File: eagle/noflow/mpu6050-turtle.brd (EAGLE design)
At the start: 52.4 x 77.6 mm, 21 parts

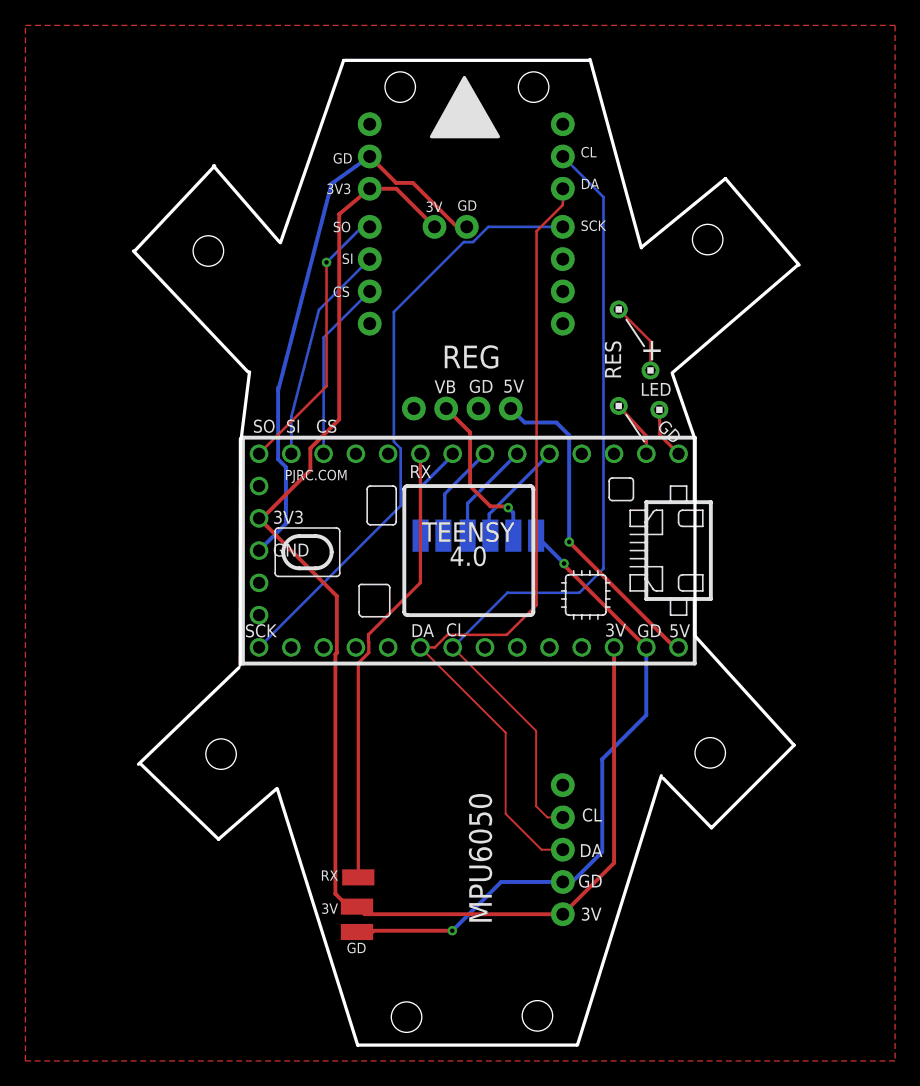
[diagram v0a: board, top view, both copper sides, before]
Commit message: Added no-flow board
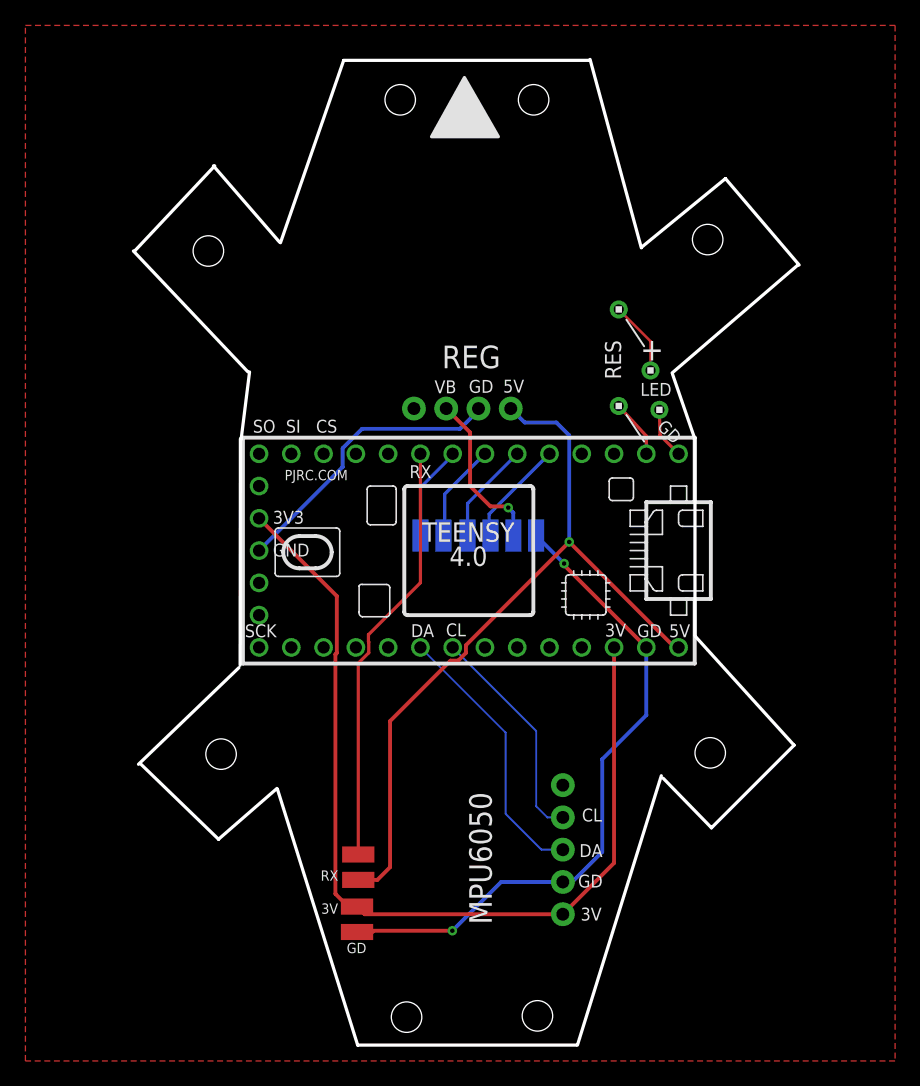
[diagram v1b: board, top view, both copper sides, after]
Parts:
- removed PMW1, PMW2: (no value), SparkFun-Connectors:1X04_NO_SILK
- removed PMW3: (no value), SparkFun-Connectors:1X02_NO_SILK
- removed VL1, VL2: (no value), SparkFun-Connectors:1X03_NO_SILK
- added 3V1: (no value), wirepad:SMD1,27-2,54
- moved RX 1.80 mm to (26.0, 16.0)
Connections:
- net 3V3: no longer PMW3.1, VL2.1
- net 5V: now also 3V1.1
- net CS: no longer PMW2.3
- net GND: no longer PMW3.2, VL2.2
- net MISO: no longer PMW2.1
- net MOSI: no longer PMW2.2
- net SCK: no longer PMW1.1
- net SCL: no longer VL1.2
- net SDA: no longer VL1.1
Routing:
- net SCL: track 65.9 -> 17.7 mm
- net SCK: track 47.6 -> 0.29 mm
- net SDA: track 65.7 -> 21.5 mm
- net 3V3: track 110.0 -> 74.1 mm
- net 5V: track 25.8 -> 60.0 mm
- net MISO: track 21.8 -> 0.00 mm, vias 1 -> 0
- net GND: track 97.5 -> 75.9 mm
- net MOSI: track 17.3 -> 0.00 mm
- net CS: track 14.3 -> 0.00 mm
- net RX: track 35.4 -> 33.6 mm
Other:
- board text removed: "PMW3901"
- board text removed: "VL53LL1"

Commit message: modified:   eagle/noflow/mpu6050-turtle.brd
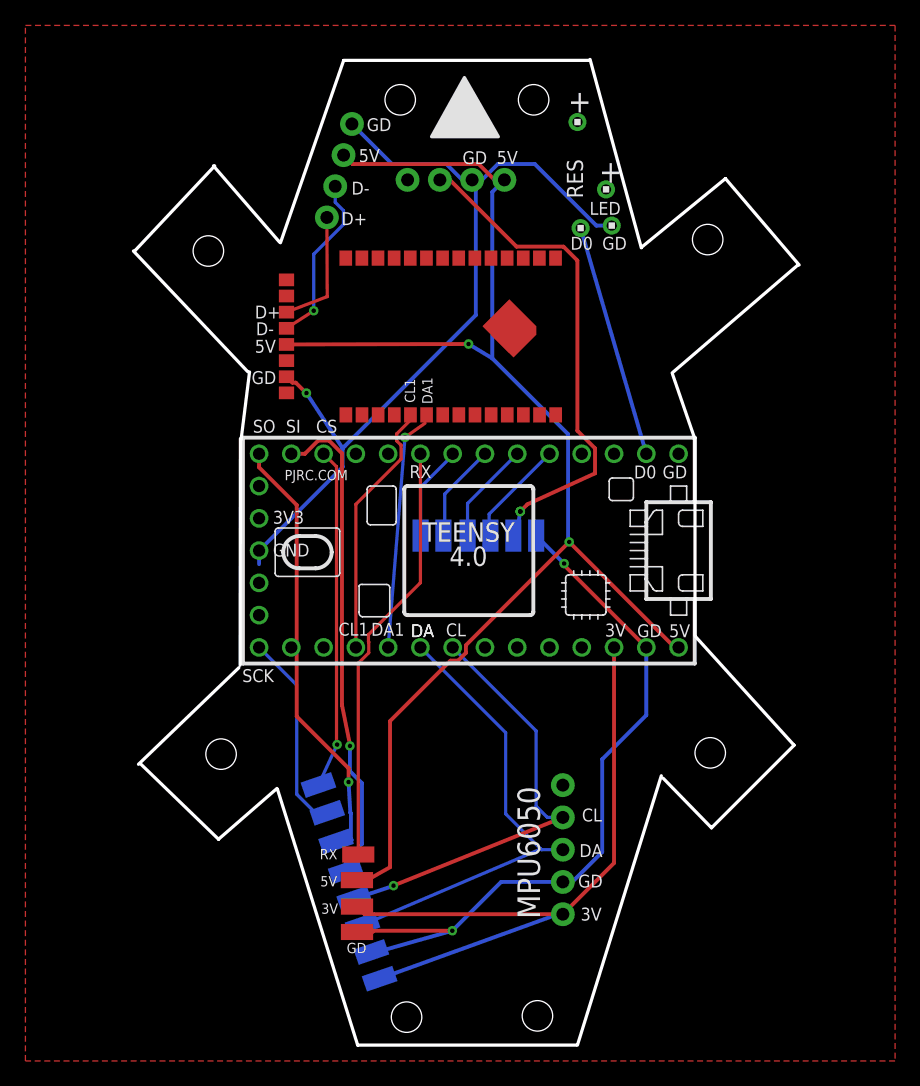
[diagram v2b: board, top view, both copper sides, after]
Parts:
- added 3V2, 3V3, CS, GD1, GD2, RX1, RX2, SCK: (no value), wirepad:SMD1,27-2,54
- added J2: (no value), SparkFun-Connectors:1X04_NO_SILK
- added U$2: TINYPICO-NANO-CONNECTOR, TinyPICO_NANO_Eagle:TINYPICO-NANO-CONNECTOR
- moved REG 18.0 mm to (37.5, 69.1)
- moved U$4 15.1 mm to (43.2, 73.7)
- moved U$7 15.0 mm to (46.0, 65.5)
- moved U$6 14.7 mm to (45.5, 68.3)
- moved U$3 14.3 mm to (43.5, 65.3)
- moved 3V1 0.11 mm to (25.9, 14.0)
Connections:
- removed net VBAT: REG.3, VBAT.1
- new net D+: J2.4, U$2.D+
- new net D-: J2.3, U$2.D-
- new net SCL1: U$1.16/A2, U$2.IO22
- new net SDA1: U$1.17/A3, U$2.IO21
- new net VB: REG.3, U$2.VBAT, VBAT.1
- net 3V3: now also 3V2.1, U$2.3V3; no longer U$1.3V3_LN
- net 5V: now also J2.2, U$2.5V
- net CS: now also CS.1
- net G2: no longer U$7.1
- net GND: now also GD1.1, J2.1, U$2.GND$1, U$2.GND$2, U$2.GND$3, U$2.GND$4, U$7.1
- net MISO: now also 3V3.1
- net MOSI: now also RX2.1
- net SCK: now also SCK.1
- net SCL: now also GD2.1
- net SDA: now also RX1.1
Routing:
- net GND: track 75.9 -> 129.1 mm, vias 2 -> 3
- net 5V: track 60.0 -> 107.4 mm, vias 1 -> 2
- net VB: track 0.00 -> 38.9 mm, vias 0 -> 2
- net MOSI: track 0.00 -> 38.7 mm, vias 0 -> 1
- net MISO: track 0.00 -> 33.4 mm, vias 0 -> 1
- net CS: track 0.00 -> 26.8 mm, vias 0 -> 1
- net SCL1: track 0.00 -> 20.4 mm
- net 3V3: track 74.1 -> 55.3 mm
- net SDA1: track 0.00 -> 18.5 mm, vias 0 -> 1
- net SCL: track 17.7 -> 35.3 mm, vias 0 -> 1
- net SCK: track 0.29 -> 15.8 mm
- net SDA: track 21.5 -> 36.8 mm
- net LED_R_IN: track 4.61 -> 18.5 mm
- net D-: track 0.00 -> 13.6 mm, vias 0 -> 1
- net VBAT: track 12.9 -> 0.00 mm, vias 1 -> 0
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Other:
- board text added: "CL1"
- board text added: "D+"
- board text added: "D-"
- board text added: "D0"
- board text added: "DA1"
